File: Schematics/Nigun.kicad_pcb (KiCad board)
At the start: 2 copper layers, 101.6 x 50.8 mm, 146 parts, among them J1 USB-MICRO-B, J2 RF_INPUT, J3 RF_OUTPUT, P1 CONN_02X04, P2 CONN_SWD, SW1 SW_PUSH_SMALL_H, T1 TC1-1-43A+, T2 TC4-1W+, U1 STF202, U2 SKY13351, U3 MIC5504-3.3YM5-TR, U4 AP7365-WG-7, U5 LP0805A0881AS, U6 ADRF6612, U7 FOX924B-16.000, U8 SKY13373, U9 ATSAMD21E

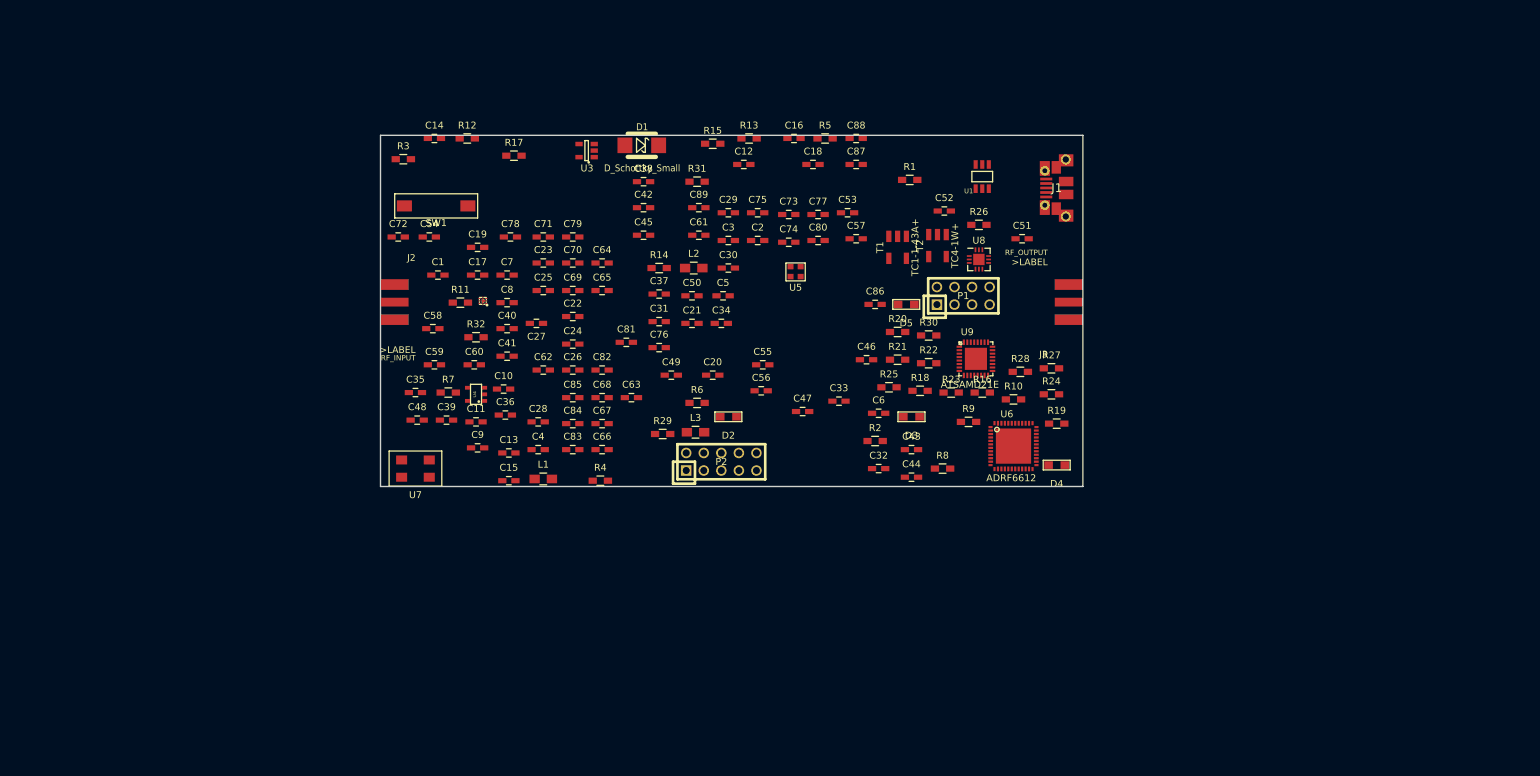
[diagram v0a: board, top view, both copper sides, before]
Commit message: replaced 45deg bent RF traces with curvy traces
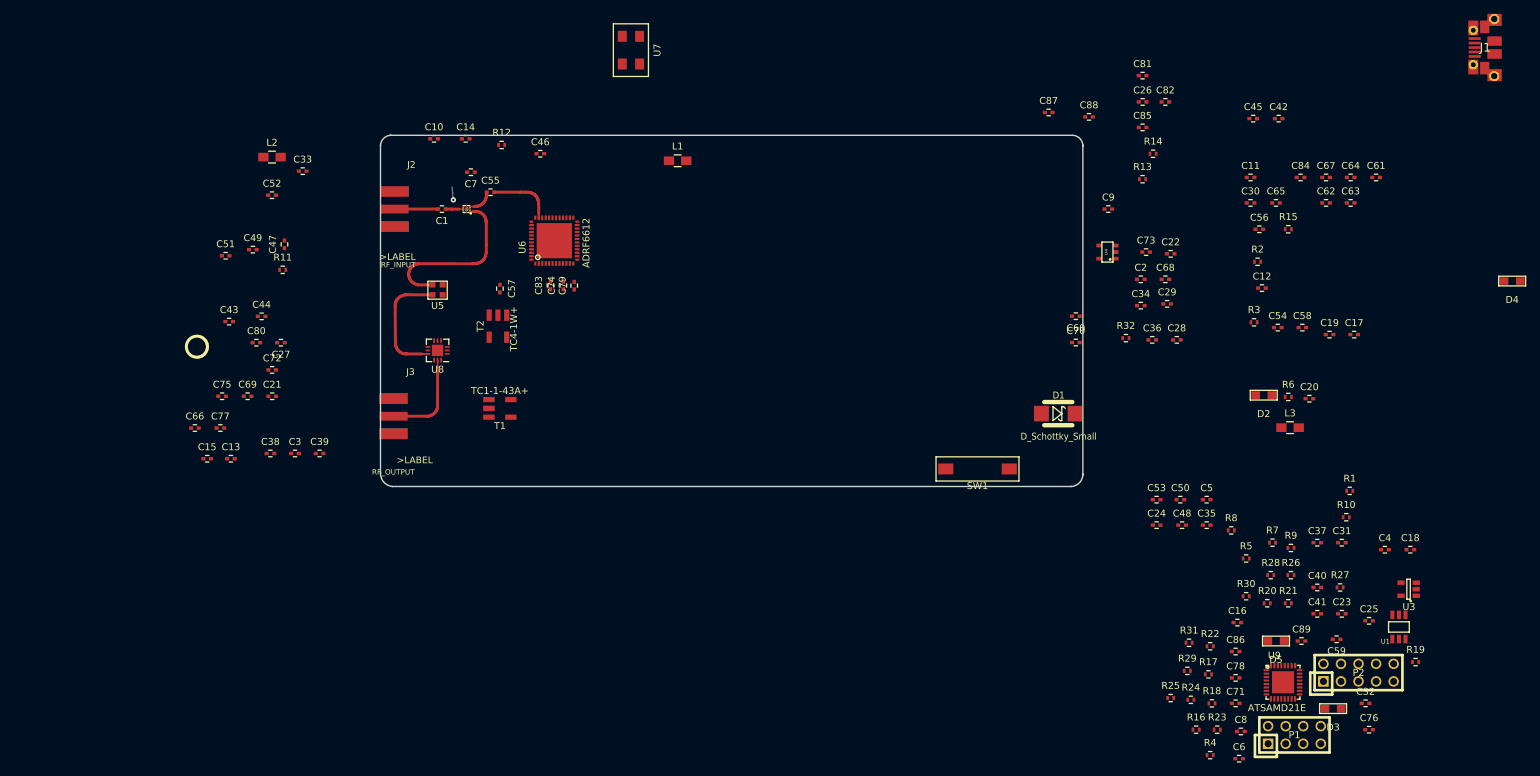
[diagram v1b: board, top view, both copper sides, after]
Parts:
- C1, C10, C11, C12, C13, C14, C15, C16, C17, C18, C19, C2, C20, C21, C22, C23, C24, C25, C26, C27, C28, C29, C3, C30, C31, C32, C33, C34, C35, C36, C37, C38, C39, C4, C40, C41, C42, C43, C44, C45, C46, C47, C48, C49, C5, C50, C51, C52, C53, C54, C55, C56, C57, C58, C59, C6, C60, C61, C62, C63, C64, C65, C66, C67, C68, C69, C7, C70, C71, C72, C73, C74, C75, C76, C77, C78, C79, C8, C80, C81, C82, C83, C84, C85, C86, C87, C88, C89, C9: footprint Capacitors_SMD:C_0603_HandSoldering -> Capacitors_SMD:C_0402
- R1, R10, R11, R12, R13, R14, R15, R16, R17, R18, R19, R2, R20, R21, R22, R23, R24, R25, R26, R27, R28, R29, R3, R30, R31, R32, R4, R5, R6, R7, R8, R9: footprint Resistors_SMD:R_0603_HandSoldering -> Resistors_SMD:R_0402
- moved C59 136.4 mm to (253.7, 115.2), turned to 180 degrees
- moved U3 134.8 mm to (264.2, 108.0)
- moved C25 128.7 mm to (258.4, 112.5)
- moved C17 127.1 mm to (256.3, 71.1)
- moved C23 126.2 mm to (254.5, 111.5)
- moved C58 125.8 mm to (248.8, 70.1)
- moved R17 125.4 mm to (235.2, 120.3)
- moved R3 125.3 mm to (241.8, 69.3)
- moved C19 123.9 mm to (252.7, 71.1)
- moved C54 123.4 mm to (245.2, 70.1)
- moved C4 123.3 mm to (260.7, 102.2)
- moved C40 123.0 mm to (251.0, 107.7)
- moved C41 123.0 mm to (251.0, 111.5)
- moved C8 122.9 mm to (239.9, 128.5)
- moved C78 122.8 mm to (239.1, 120.8)
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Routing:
- net Net-(U2-Pad1): track 0.00 -> 25.1 mm
- net Net-(U5-PadOUT): track 0.00 -> 17.2 mm
- net Net-(J3-PadP): track 0.00 -> 13.9 mm
- net Net-(C55-Pad2): track 0.00 -> 9.59 mm
- net Net-(C1-Pad2): track 0.00 -> 6.34 mm
- net (no net): track 0.00 -> 6.19 mm, vias 0 -> 1
- net Net-(C55-Pad1): track 0.00 -> 3.79 mm
- net Net-(C1-Pad1): track 0.00 -> 2.52 mm
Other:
- outline, holes or cut-outs redrawn
- copper layers 2 -> 4
- net class Default: clearance 0.2 -> 0.1524; trace_width 0.25 -> 0.1524; via_dia 0.6 -> 0.4572; via_drill 0.4 -> 0.3048
- rule trace_clearance: 0.2 -> 0.1524
- rule trace_min: 0.2 -> 0.1524

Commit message: PCB design update - finished RF traces and 2 sides of 6612
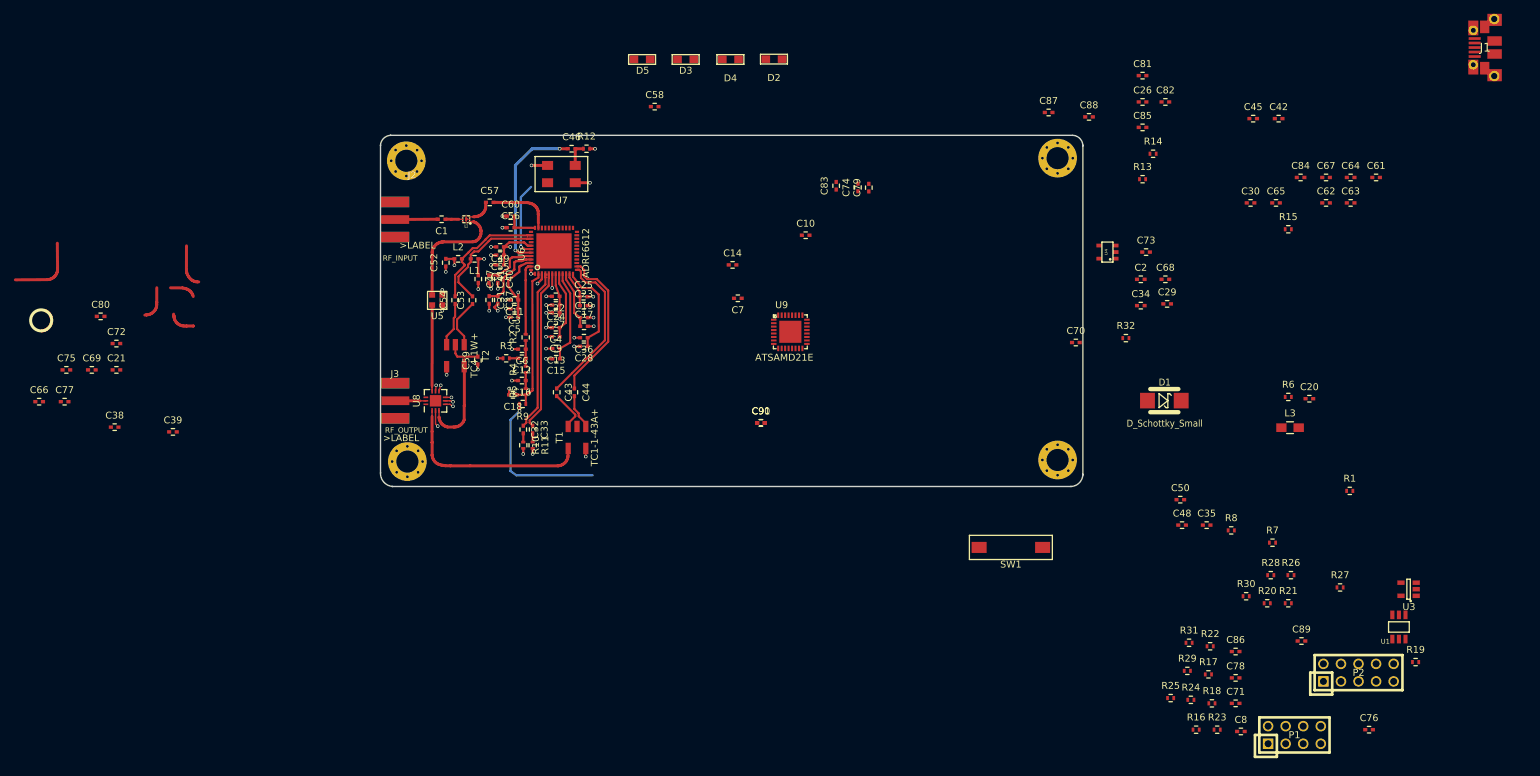
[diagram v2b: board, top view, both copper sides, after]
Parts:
- added C90: 10uF, Footprints:C_0402_inv_value, F.Cu at (170.5, 83.9)
- added C91: 100nF, Footprints:C_0402_inv_value, F.Cu at (170.5, 83.9)
- added J4: MOUNTING_HOLE, Footprints:MOUNTING_HOLE-126MIL-COPPER, F.Cu at (213.4, 89.3)
- added J4: MOUNTING_HOLE, Footprints:MOUNTING_HOLE-126MIL-COPPER, F.Cu at (213.4, 45.6)
- added J4: MOUNTING_HOLE, Footprints:MOUNTING_HOLE-126MIL-COPPER, F.Cu at (119.2, 46.0)
- added J4: MOUNTING_HOLE, Footprints:MOUNTING_HOLE-126MIL-COPPER, F.Cu at (119.3, 89.5)
- C1, C10, C11, C12, C13, C14, C15, C16, C17, C18, C19, C2, C20, C21, C22, C23, C24, C25, C26, C27, C28, C29, C3, C30, C31, C32, C33, C34, C35, C36, C37, C38, C39, C4, C40, C41, C42, C43, C44, C45, C46, C5, C52, C6, C61, C63, C66, C69, C7, C71, C73, C77, C8, C82, C83, C85, C89, C9: footprint Capacitors_SMD:C_0402 -> Footprints:C_0402_inv_value
- C47: value 1000pF -> 150pF; footprint Capacitors_SMD:C_0402 -> Footprints:C_0402_inv_value
- C48: value 10pF -> 1000pF; footprint Capacitors_SMD:C_0402 -> Footprints:C_0402_inv_value
- C49, C56: value 1000pF -> 10pF; footprint Capacitors_SMD:C_0402 -> Footprints:C_0402_inv_value
- C50: value 0.1uF -> 1000pF; footprint Capacitors_SMD:C_0402 -> Footprints:C_0402_inv_value
- C51: value 150pF -> 0.1uF; footprint Capacitors_SMD:C_0402 -> Footprints:C_0402_inv_value
- C53: value 10uF -> 150pF; footprint Capacitors_SMD:C_0402 -> Footprints:C_0402_inv_value
- C54, C59: value 10pF -> 150pF; footprint Capacitors_SMD:C_0402 -> Footprints:C_0402_inv_value
- C55: value 22pF -> 10uF; footprint Capacitors_SMD:C_0402 -> Footprints:C_0402_inv_value
- C57: value 150pF -> 22pF; footprint Capacitors_SMD:C_0402 -> Footprints:C_0402_inv_value
- C58: value 10nF -> 1000pF; footprint Capacitors_SMD:C_0402 -> Footprints:C_0402_inv_value
- C60: value 10000pF -> 10nF; footprint Capacitors_SMD:C_0402 -> Footprints:C_0402_inv_value
- C62: value 10pF -> 10000pF; footprint Capacitors_SMD:C_0402 -> Footprints:C_0402_inv_value
- C64, C65, C72, C79: value 0.1uF -> 10pF; footprint Capacitors_SMD:C_0402 -> Footprints:C_0402_inv_value
- C67, C68, C81, C84: value 10uF -> 0.1uF; footprint Capacitors_SMD:C_0402 -> Footprints:C_0402_inv_value
- C70, C75: value 10pF -> 10uF; footprint Capacitors_SMD:C_0402 -> Footprints:C_0402_inv_value
- C74: value 10pF -> 0.1uF; footprint Capacitors_SMD:C_0402 -> Footprints:C_0402_inv_value
- C76: value 100pF -> 10pF; footprint Capacitors_SMD:C_0402 -> Footprints:C_0402_inv_value
- C78: value 100nF -> 100pF; footprint Capacitors_SMD:C_0402 -> Footprints:C_0402_inv_value
- C80: value 0.1uF -> 100nF; footprint Capacitors_SMD:C_0402 -> Footprints:C_0402_inv_value
- C86: value 1uF -> 10uF; footprint Capacitors_SMD:C_0402 -> Footprints:C_0402_inv_value
- C87: value 100nF -> 10uF; footprint Capacitors_SMD:C_0402 -> Footprints:C_0402_inv_value
- C88: value 10uF -> 1uF; footprint Capacitors_SMD:C_0402 -> Footprints:C_0402_inv_value
- L1, L2: footprint Capacitors_SMD:C_0805_HandSoldering -> Footprints:C_0402_inv_value
- T1: footprint Footprints:AT224-1A -> AT224-1A
- moved D3 132.6 mm to (159.6, 31.3)
- moved C18 131.7 mm to (134.6, 79.8), turned to 180 degrees
- moved C59 130.6 mm to (129.5, 74.9), turned to 90 degrees
- moved C41 129.2 mm to (131.1, 63.1), turned to 270 degrees
- moved C31 128.2 mm to (131.2, 66.1), turned to 270 degrees
- moved C32 128.1 mm to (136.1, 84.9), turned to 270 degrees
- moved C40 126.6 mm to (132.4, 63.1), turned to 270 degrees
- moved D5 124.4 mm to (153.3, 31.3)
- moved C4 124.2 mm to (140.8, 70.1), turned to 180 degrees
- moved C37 123.6 mm to (132.4, 66.1), turned to 270 degrees
- moved C25 122.9 mm to (144.8, 65.6)
- moved R10 119.5 mm to (136.1, 87.1), turned to 270 degrees
- moved C6 119.5 mm to (135.9, 73.2), turned to 180 degrees
- moved C54 119.1 mm to (126.2, 66.1), turned to 90 degrees
- moved C23 118.4 mm to (144.8, 66.9)
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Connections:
- net Net-(C32-Pad1) renamed /EXTVCOIN+
- net Net-(C33-Pad1) renamed /EXTVCOIN-
- net Net-(C43-Pad1) renamed /LOOUT+
- net Net-(C43-Pad2) renamed /TC1IN+
- net Net-(C44-Pad1) renamed /LOOUT-
- net Net-(C44-Pad2) renamed /TC1IN-
- C47 pad 1: Net-(C47-Pad1) -> /VCC_3.7V
- C47 pad 2: Net-(C47-Pad2) -> Earth
- C48 pad 1: /VCC_3.7V -> /IFOUT2+
- C48 pad 2: Earth -> Net-(C48-Pad2)
- C49 pad 1: Net-(C49-Pad1) -> /VCC_3.7V
- C49 pad 2: Net-(C49-Pad2) -> Earth
- C50 pad 1: /VCC_3.7V -> /IFOUT2-
- C50 pad 2: Earth -> Net-(C50-Pad2)
- C51 pad 1: Net-(C51-Pad1) -> /VCC_3.7V
- C51 pad 2: Net-(C51-Pad2) -> Earth
- C52 pad 1: Net-(C52-Pad1) -> Earth
- C52 pad 2: Net-(C52-Pad2) -> /VCC_3.7V
- C53 pad 1: /VCC_3.7V -> /TC4IN+
- C53 pad 2: Earth -> /IFOUT1+
- C54 pad 1: Earth -> /TC4IN-
- C54 pad 2: Net-(C54-Pad2) -> /IFOUT1-
- C55 pad 1: Net-(C55-Pad1) -> /VCC_3.7V
- C55 pad 2: Net-(C55-Pad2) -> Earth
- C56 pad 1: Net-(C56-Pad1) -> Earth
- C57 pad 1: Earth -> Net-(C57-Pad1)
- C58 pad 1: Earth -> Net-(C58-Pad1)
- C58 pad 2: Net-(C54-Pad2) -> Net-(C58-Pad2)
- C59 pad 1: Net-(C59-Pad1) -> Earth
- C59 pad 2: Earth -> Net-(C59-Pad2)
- C60 pad 1: Net-(C59-Pad1) -> Earth
- C60 pad 2: Earth -> Net-(C56-Pad2)
- C61 pad 1: /VCC_3.7V -> Net-(C61-Pad1)
- C62 pad 1: /VCC_3.7V -> Net-(C61-Pad1)
- C71 pad 1: Net-(C71-Pad1) -> /VCC_3.7V
- C73 pad 1: /VCC_3.7V -> Net-(C73-Pad1)
- C76 pad 1: Net-(C76-Pad1) -> /VCC_3.7V
- C78 pad 1: Net-(C71-Pad1) -> Net-(C78-Pad1)
- C80 pad 1: /VCC_3.7V -> Net-(C73-Pad1)
- C81 pad 1: Net-(C76-Pad1) -> /VCC_3.7V
- C83 pad 1: /VCC_3.7V -> Net-(C78-Pad1)
- C86 pad 1: Net-(C86-Pad1) -> /VCC_3.7V
- C87 pad 1: /MCU_VDDIN -> /VCC_3.7V
- C88 pad 1: /MCU_VDDIN -> Net-(C88-Pad1)
- C89 pad 1: /!RESET -> /MCU_VDDIN
- L1 pad 2: Net-(C52-Pad2) -> /IFOUT1+
- L2 pad 2: Net-(C51-Pad2) -> /IFOUT1-
- R13 pad 1: Net-(C47-Pad2) -> Net-(C48-Pad2)
- R14 pad 1: Net-(C49-Pad2) -> Net-(C50-Pad2)
- R15 pad 1: Net-(C56-Pad2) -> Net-(C58-Pad2)
- R17 pad 1: Net-(C71-Pad1) -> Net-(C73-Pad1)
- T1 pad 4: Net-(T1-Pad4) -> Earth
- T1 pad 6: Earth -> Net-(T1-Pad6)
- T2 pad 1: Net-(C51-Pad1) -> /TC4IN+
- T2 pad 2: Net-(C57-Pad2) -> Net-(C59-Pad2)
- T2 pad 3: Net-(C52-Pad1) -> /TC4IN-
- U2 pad 3: Net-(C55-Pad1) -> Net-(C57-Pad1)
- U6 pad 22: Net-(C47-Pad1) -> /IFOUT2+
- U6 pad 23: Net-(C49-Pad1) -> /IFOUT2-
- U6 pad 25: Net-(C59-Pad1) -> Net-(C61-Pad1)
- U6 pad 26: Net-(C56-Pad1) -> Net-(C58-Pad1)
- U6 pad 30: Net-(C76-Pad1) -> Net-(C78-Pad1)
- U6 pad 35: Net-(C55-Pad2) -> Net-(C57-Pad2)
- U6 pad 36: Net-(C54-Pad2) -> Net-(C56-Pad2)
- U6 pad 38: Net-(C51-Pad2) -> /IFOUT1-
- U6 pad 39: Net-(C52-Pad2) -> /IFOUT1+
- U8 pad 1: Net-(T2-Pad6) -> Net-(T1-Pad6)
- U8 pad 3: Net-(T1-Pad4) -> Net-(T2-Pad6)
- U9 pad 29: Net-(C86-Pad1) -> Net-(C88-Pad1)
- U9 pad 9: Net-(C71-Pad1) -> Net-(C73-Pad1)
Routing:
- net Earth: track 0.04 -> 44.5 mm, vias 0 -> 46
- net /VCC_3.7V: track 0.00 -> 31.4 mm, vias 0 -> 5
- net Net-(T1-Pad6): track 0.00 -> 28.9 mm
- net (no net): track 6.19 -> 34.1 mm, vias 1 -> 0
- net /EXTVCOIN+: track 0.00 -> 23.5 mm
- net /EXTVCOIN-: track 0.00 -> 23.5 mm
- net Net-(C46-Pad1): track 0.00 -> 23.2 mm, vias 0 -> 2
- net /LOOUT+: track 0.00 -> 22.8 mm
- net /LOOUT-: track 0.00 -> 22.7 mm
- net ADRF_VTUNE: track 0.00 -> 22.3 mm, vias 0 -> 1
- net Net-(C18-Pad1): track 0.00 -> 21.3 mm
- net /IFOUT1-: track 0.00 -> 17.6 mm
- net /IFOUT1+: track 0.00 -> 17.4 mm
- net Net-(T2-Pad6): track 0.00 -> 14.6 mm
- net Net-(C28-Pad1): track 0.00 -> 13.7 mm
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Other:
- net class Default: via_dia 0.4572 -> 0.508; via_drill 0.3048 -> 0.3302

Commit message: Place and route updates
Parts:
- removed C2, C21: 10uF, Footprints:C_0402_inv_value
- removed J4 (x4): MOUNTING_HOLE, Footprints:MOUNTING_HOLE-126MIL-COPPER
- removed U1: STF202, hack-footprints:TSOP-6
- added D6: PRTR5V0U2X, Footprints:SOT143B, F.Cu at (158.7, 53.6)
- C1, C10, C11, C12, C13, C14, C15, C16, C17, C18, C19, C20, C22, C23, C24, C25, C26, C27, C28, C29, C3, C30, C31, C32, C33, C34, C35, C36, C37, C38, C39, C4, C40, C41, C42, C43, C44, C45, C46, C47, C48, C49, C5, C50, C51, C52, C53, C54, C55, C56, C57, C58, C59, C6, C60, C61, C62, C63, C64, C65, C66, C67, C68, C69, C7, C70, C71, C72, C73, C74, C75, C76, C77, C78, C79, C8, C80, C81, C82, C83, C84, C85, C86, C87, C88, C89, C9, C90, C91, L1, L2: footprint Footprints:C_0402_inv_value -> Capacitors_SMD:C_0402
- J1: footprint gsg-modules:USB-MICROB-FCI-10103592-EXT -> Footprints:FRAMATOME_10118194-0001LF
- T1: footprint AT224-1A -> Footprints:AT224-1A
- moved C76 146.6 mm to (136.1, 47.6), turned to 180 degrees
- moved C8 134.4 mm to (126.7, 56.0), turned to 270 degrees
- moved C71 132.1 mm to (133.5, 45.2), turned to 180 degrees
- moved C86 123.6 mm to (138.6, 45.1), turned to 180 degrees
- moved C78 123.2 mm to (142.0, 45.1)
- moved C64 120.3 mm to (135.5, 51.3), turned to 270 degrees
- moved C67 117.9 mm to (134.3, 51.3), turned to 270 degrees
- moved R19 114.2 mm to (159.2, 76.1), turned to 180 degrees
- moved J1 113.4 mm to (166.5, 51.9), turned to 90 degrees
- moved U3 113.0 mm to (160.2, 63.7), turned to 270 degrees
- moved C61 112.6 mm to (147.0, 54.2)
- moved C65 111.6 mm to (133.5, 47.6), turned to 180 degrees
- moved C63 108.8 mm to (147.0, 50.6), turned to 180 degrees
- moved R27 108.2 mm to (151.3, 74.5), turned to 180 degrees
- moved C84 106.6 mm to (141.9, 49.3), turned to 180 degrees
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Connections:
- J1 pad 2: Net-(J1-Pad2) -> USB_D-
- J1 pad 3: Net-(J1-Pad3) -> USB_D+
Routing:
- net /VCC_3.7V: track 31.4 -> 166.5 mm, vias 5 -> 24
- net Earth: track 44.5 -> 121.6 mm, vias 46 -> 130
- net IN_SW_VCTL2: track 0.00 -> 72.7 mm, vias 0 -> 2
- net /VCC_3.3V: track 3.23 -> 55.6 mm, vias 2 -> 4
- net ADRF_MUXOUT: track 10.9 -> 52.7 mm, vias 1 -> 4
- net IN_SW_VCTL1: track 0.00 -> 41.7 mm, vias 0 -> 2
- net OUT_SW_V2: track 1.15 -> 41.7 mm, vias 1 -> 4
- net ADRF_CSNOT: track 0.00 -> 38.9 mm, vias 0 -> 2
- net OUT_SW_V1: track 1.22 -> 36.5 mm, vias 1 -> 2
- net (no net): track 34.1 -> 0.01 mm
- net USB_D+: track 0.00 -> 34.1 mm, vias 0 -> 2
- net USB_D-: track 0.00 -> 32.7 mm, vias 0 -> 2
- net ADRF_SDIO: track 0.00 -> 29.2 mm, vias 0 -> 2
- net ADRF_SCLK: track 0.00 -> 28.2 mm, vias 0 -> 4
- net SWDCLK: track 0.00 -> 24.4 mm
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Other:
- board size 101.6 x 50.8 mm -> 53.9 x 50.8 mm
- net class Differential pair added: clearance 0.1524, trace_width 0.3302, via_dia 0.508, via_drill 0.3302

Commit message: Finished front layer
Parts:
- R29: value 0 -> 1k
- moved C91 1.80 mm to (148.2, 87.9)
- moved R32 1.80 mm to (148.3, 89.4)
- moved C46 0.71 mm to (155.4, 44.4)
- moved R12 0.71 mm to (157.6, 44.4)
- moved R18 0.36 mm to (160.8, 79.3)
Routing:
- net IN_SW_VCTL1: track 41.7 -> 134.5 mm, vias 2 -> 3
- net OUT_SW_V1: track 36.5 -> 78.1 mm, vias 2 -> 5
- net /VCC_3.3V: track 55.6 -> 78.2 mm, vias 4 -> 5
- net SWDIO: track 0.00 -> 22.5 mm, vias 0 -> 4
- net IN_SW_VCTL2: track 72.7 -> 93.9 mm, vias 2 -> 6
- net /MCU_VDDIN: track 21.5 -> 37.1 mm, vias 3 -> 4
- net ADRF_SCLK: track 28.2 -> 43.6 mm
- net ADRF_CSNOT: track 38.9 -> 52.8 mm, vias 2 -> 3
- net OUT_SW_V2: track 41.7 -> 53.9 mm, vias 4 -> 5
- net ADRF_SDIO: track 29.2 -> 39.8 mm
- net ADRF_VTUNE: track 21.9 -> 29.1 mm
- net SWDCLK: track 24.4 -> 22.0 mm
- net USB_D-: track 32.7 -> 34.7 mm, vias 2 -> 0
- net USB_D+: track 34.1 -> 35.7 mm, vias 2 -> 0
- net Net-(U7-Pad1): track 0.00 -> 1.37 mm
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
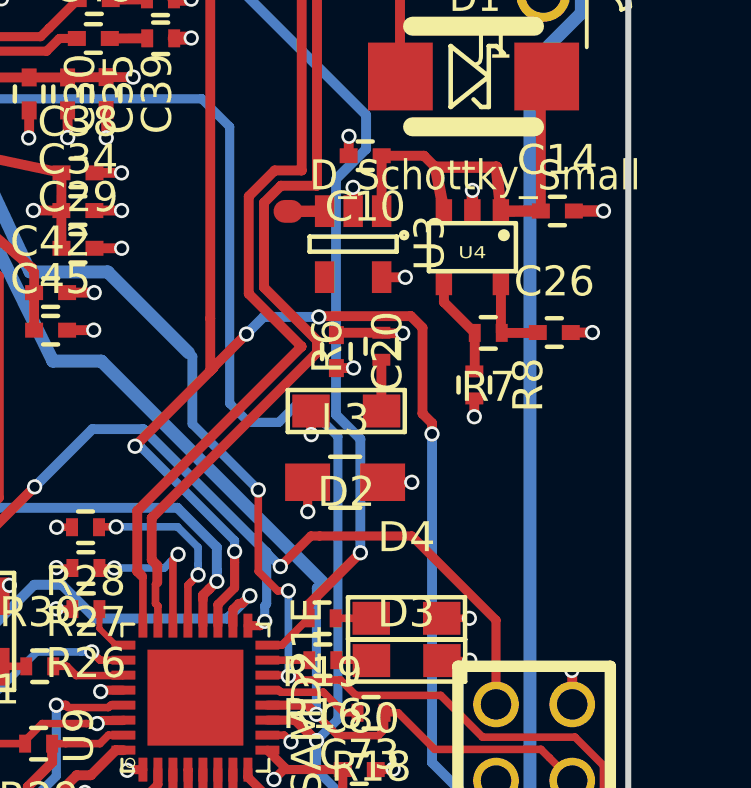
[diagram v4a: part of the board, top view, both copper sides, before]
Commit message: added large inductor at the MCU powe input
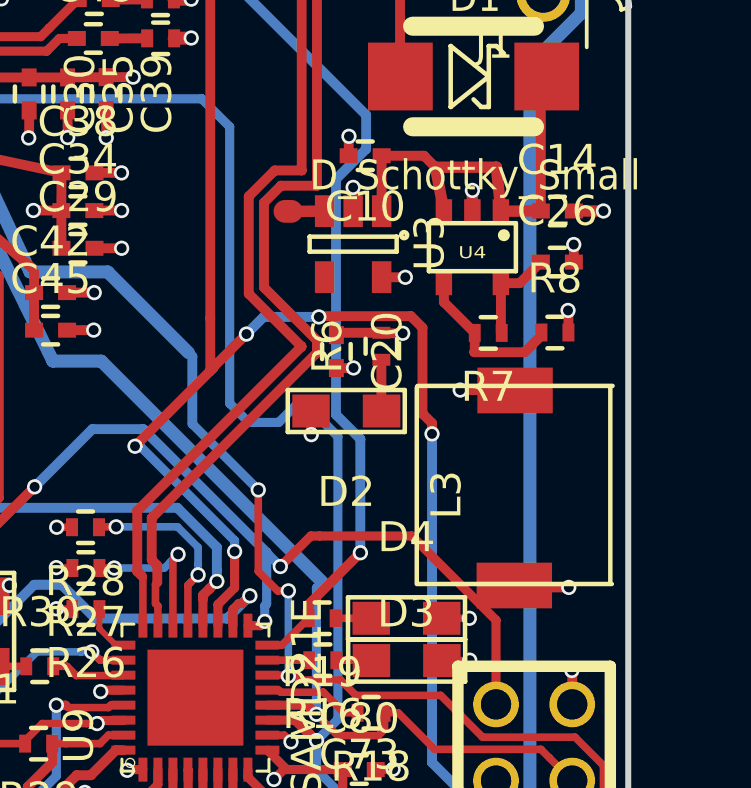
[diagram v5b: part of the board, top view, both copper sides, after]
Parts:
- L3: footprint Capacitors_SMD:C_0805_HandSoldering -> SRR0603-100ML
- moved L3 5.76 mm to (165.7, 72.0), turned to 90 degrees
- moved R8 3.20 mm to (166.9, 66.6), turned to 0 degrees
- moved C26 2.35 mm to (167.0, 64.3)
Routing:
- net /MCU_VDDIN: track 37.1 -> 47.7 mm
- net Net-(R7-Pad2): track 3.37 -> 5.30 mm
- net /VCC_3.3V: track 78.2 -> 76.5 mm
